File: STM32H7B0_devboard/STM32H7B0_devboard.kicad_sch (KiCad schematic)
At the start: 83 parts, among them J1 SWD, J2 24LC512 socet, J4 PORT_A, J5 PORT_B, J6 PORT_C, J7 PORT_D, J8 PORT_E, J9 Power_Conn, Q1 S8050, SW1 BOOT_SEL, U1 STM32H7B0VBT6, Y1 32.768KHz, Y2 25MHz

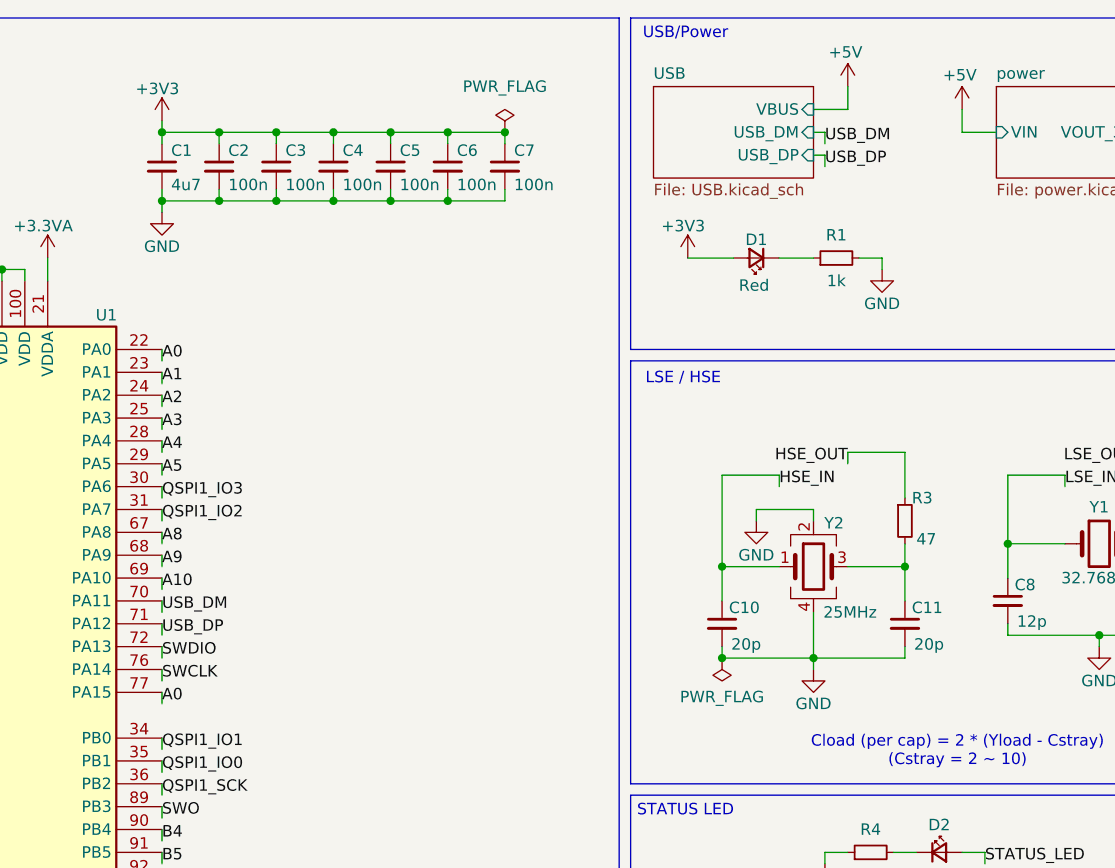
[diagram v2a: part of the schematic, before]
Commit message: Updated .gitignore
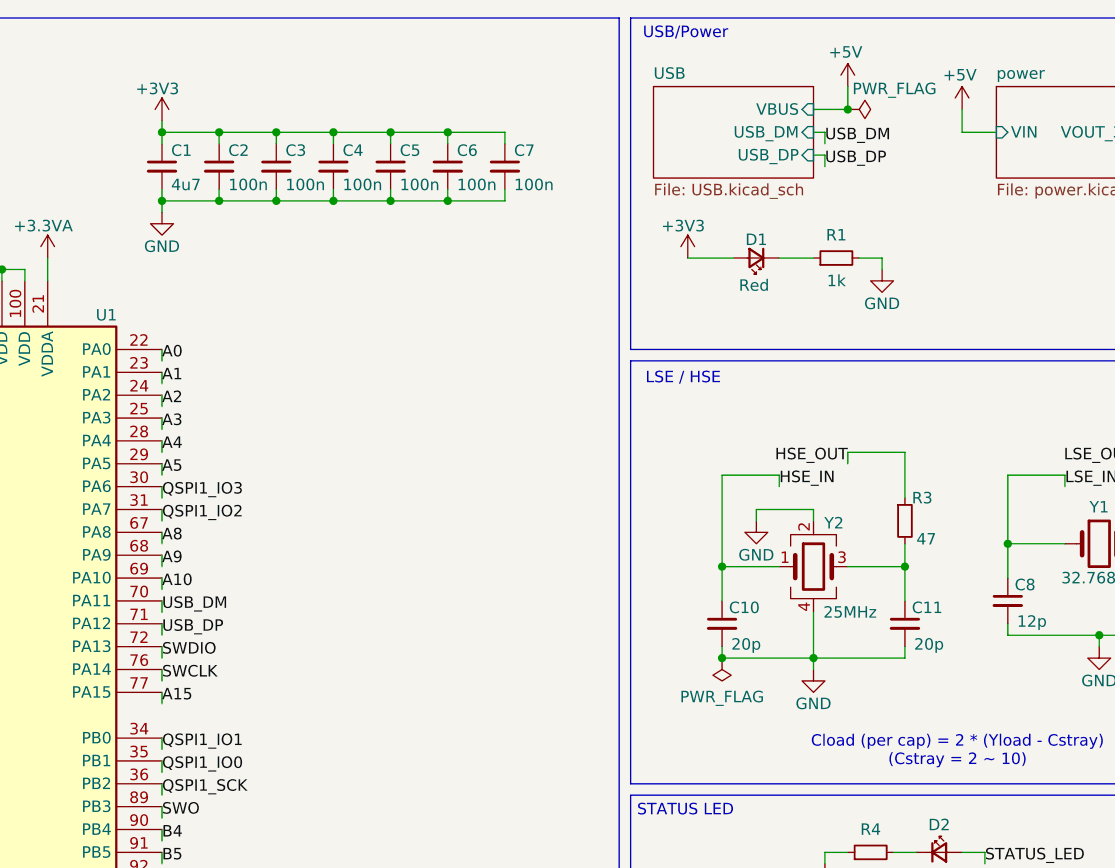
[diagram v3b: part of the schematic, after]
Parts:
- C14, C15: footprint Capacitor_SMD:C_1206_3216Metric -> Capacitor_SMD:C_0402_1005Metric
- R1, R4: footprint Resistor_SMD:R_0402_1005Metric -> Resistor_SMD:R_0603_1608Metric
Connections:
- net A0: no longer U1.77 (PA15)
- net A15: now also U1.77 (PA15)
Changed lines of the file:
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@@
 	)
 	(junction
-		(at 123.19 25.4)
-		(diameter 0)
-		(color 0 0 0 0)
-	)
-	(junction
 		(at 38.1 212.09)
 		(diameter 0)
@@
 	)
 	(junction
+		(at 161.29 22.86)
+		(diameter 0)
+		(color 0 0 0 0)
+	)
+	(junction
 		(at 49.53 269.24)
 		(diameter 0)
@@
 		)
 	)
-	(label "A0"
+	(label "A15"
 		(at 85.09 88.9 0)
 		(fields_autoplaced yes)
@@
 			)
 		)
-		(property "Footprint" "Resistor_SMD:R_0402_1005Metric"
+		(property "Footprint" "Resistor_SMD:R_0603_1608Metric"
 			(at 160.02 39.37 0)
 			(effects
@@
 	)
 	(symbol
+		(lib_id "power:PWR_FLAG")
+		(at 161.29 22.86 270)
+		(unit 1)
+		(exclude_from_sim no)
+		(in_bom yes)
+		(on_board yes)
+		(dnp no)
+		(property "Reference" "#FLG07"
+			(at 163.195 22.86 0)
+			(effects
+				(font
+					(size 1.27 1.27)
+				)
+				(hide yes)
+			)
+		)
+		(property "Value" "PWR_FLAG"
+			(at 161.798 20.574 90)
+			(effects
+				(font
+					(size 1.27 1.27)
+				)
+				(justify left)
+			)
+		)
+		(property "Footprint" ""
+			(at 161.29 22.86 0)
+			(effects
+				(font
+					(size 1.27 1.27)
+				)
+				(hide yes)
+			)
+		)
+		(property "Datasheet" "~"
+			(at 161.29 22.86 0)
+			(effects
+				(font
+					(size 1.27 1.27)
+				)
+				(hide yes)
+			)
+		)
+		(property "Description" "Special symbol for telling ERC where power comes from"
+			(at 161.29 22.86 0)
+			(effects
+				(font
+					(size 1.27 1.27)
+				)
+				(hide yes)
+			)
+		)
+		(pin "1"
+		)
+		(instances
+			(project "STM32H7B0_devboard"
+				(path "/0c02ba0f-c40f-484f-a270-dfb4a249f2e6"
+					(reference "#FLG07")
+					(unit 1)
+				)
+			)
+		)
+	)
+	(symbol
 		(lib_id "Device:R_Small")
 		(at 189.23 138.43 90)
@@
 			)
 		)
-		(property "Footprint" "Capacitor_SMD:C_1206_3216Metric"
+		(property "Footprint" "Capacitor_SMD:C_0402_1005Metric"
 			(at 95.25 210.82 0)
 			(effects
@@
 	)
 	(symbol
-		(lib_id "power:PWR_FLAG")
-		(at 123.19 25.4 0)
-		(unit 1)
-		(exclude_from_sim no)
-		(in_bom yes)
-		(on_board yes)
-		(dnp no)
-		(fields_autoplaced yes)
-		(property "Reference" "#FLG01"
-			(at 123.19 23.495 0)
-			(effects
-				(font
-					(size 1.27 1.27)
-				)
-				(hide yes)
-			)
-		)
-		(property "Value" "PWR_FLAG"
-			(at 123.19 20.32 0)
-			(effects
-				(font
-					(size 1.27 1.27)
-				)
-			)
-		)
-		(property "Footprint" ""
-			(at 123.19 25.4 0)
-			(effects
-				(font
-					(size 1.27 1.27)
-				)
-				(hide yes)
-			)
-		)
-		(property "Datasheet" "~"
-			(at 123.19 25.4 0)
-			(effects
-				(font
-					(size 1.27 1.27)
-				)
-				(hide yes)
-			)
-		)
-		(property "Description" "Special symbol for telling ERC where power comes from"
-			(at 123.19 25.4 0)
-			(effects
-				(font
-					(size 1.27 1.27)
-				)
-				(hide yes)
-			)
-		)
-		(pin "1"
-		)
-		(instances
-			(project "STM32H7B0_devboard"
-				(path "/0c02ba0f-c40f-484f-a270-dfb4a249f2e6"
-					(reference "#FLG01")
-					(unit 1)
-				)
-			)
-		)
-	)
-	(symbol
 		(lib_id "Device:R_Small")
 		(at 163.83 105.41 90)
@@
 			)
 		)
-		(property "Footprint" "Resistor_SMD:R_0402_1005Metric"
+		(property "Footprint" "Resistor_SMD:R_0603_1608Metric"
 			(at 163.83 105.41 0)
 			(effects
@@
 			)
 		)
-		(property "Footprint" "Capacitor_SMD:C_1206_3216Metric"
+		(property "Footprint" "Capacitor_SMD:C_0402_1005Metric"
 			(at 95.25 207.01 0)
 			(effects

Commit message: Started on layout
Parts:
- removed J9: Power_Conn, Connector_PinSocket_2.00mm:PinSocket_2x08_P2.00mm_Vertical, symbol Connector_Generic:Conn_02x08_Row_Letter_First
- added J9: Power_Conn, Connector_PinSocket_2.00mm:PinSocket_2x08_P2.00mm_Vertical, symbol Connector_Generic:Conn_02x08_Odd_Even
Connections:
- net +3V3: now also J9.2 (Pin_2), J9.4 (Pin_4), J9.6 (Pin_6), J9.8 (Pin_8)
- net +5V: now also J9.10 (Pin_10), J9.12 (Pin_12), J9.14 (Pin_14), J9.16 (Pin_16)
- net GND: now also J9.1 (Pin_1), J9.11 (Pin_11), J9.13 (Pin_13), J9.15 (Pin_15), J9.3 (Pin_3), J9.5 (Pin_5), J9.7 (Pin_7), J9.9 (Pin_9)
- net QSPI1_NSS: now also R11.1
- net at R23.2, U3.1 (NCS): no longer R11.1
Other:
- moved on the sheet: R11, R23, R24, R25

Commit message: Routing progress
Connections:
- net USB_DM renamed USB_DN
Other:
- sheet USB ports: added USB_DN; removed USB_DM
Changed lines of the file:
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@@
 		)
 	)
-	(label "USB_DM"
+	(label "USB_DN"
 		(at 158.75 26.67 0)
 		(fields_autoplaced yes)
@@
 		)
 	)
-	(label "USB_DM"
+	(label "USB_DN"
 		(at 85.09 78.74 0)
 		(fields_autoplaced yes)
@@
 		)
 	)
-	(label "USB_DM"
+	(label "USB_DN"
 		(at 226.06 48.26 180)
 		(fields_autoplaced yes)
@@
 			)
 		)
-		(pin "USB_DM" input
-			(at 157.48 25.4 0)
+		(pin "USB_DP" input
+			(at 157.48 27.94 0)
 			(effects
 				(font
@@
 			)
 		)
-		(pin "USB_DP" input
-			(at 157.48 27.94 0)
+		(pin "USB_DN" input
+			(at 157.48 25.4 0)
 			(effects
 				(font

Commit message: Done V1
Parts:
- C1, C15: LCSC (none) -> C307423
- C10, C11: LCSC (none) -> C1554
- C12, C13: LCSC (none) -> C343040
- C14, C2, C3, C4, C5, C6, C7: LCSC (none) -> C14445
- C16: LCSC (none) -> C913556
- C17: LCSC (none) -> C60133
- C8, C9: LCSC (none) -> C1547
- D1: LCSC (none) -> C965799
- D2: LCSC (none) -> C965807
- L1: LCSC (none) -> C74308
- Q1: LCSC (none) -> C916390
- R1: LCSC (none) -> C21190
- R10, R11, R15, R16, R9: LCSC (none) -> C25933
- R12: LCSC (none) -> C2849042
- R13: LCSC (none) -> C60490
- R14: LCSC (none) -> C11702
- R17, R18, R5, R6, R7, R8: LCSC (none) -> C25152
- R2, R3: LCSC (none) -> C25118
- R23, R24, R25, R26, R27, R28: LCSC (none) -> C115304
- R4: LCSC (none) -> C25989
- SW1: LCSC (none) -> C5962834
- U1: LCSC (none) -> C730227
- U3: LCSC (none) -> C5267629
- Y1: LCSC (none) -> C5213671
- Y2: LCSC (none) -> C13740

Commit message: Finished board
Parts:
- removed SW1: BOOT_SEL, Button_Switch_SMD:Nidec_Copal_CAS-120A, symbol Switch:SW_Nidec_CAS-120A1
- added JP21, JP22: ~, Jumper:SolderJumper-2_P1.3mm_Open_TrianglePad1.0x1.5mm, symbol Jumper:SolderJumper_2_Open
- added R29: 10k, Resistor_SMD:R_0402_1005Metric, symbol Device:R_Small
- C1, C15: LCSC C307423 -> C23733
- C12, C13: LCSC C343040 -> C12530
- C14, C2, C3, C4, C5, C6, C7: LCSC C14445 -> C1525
- C16: LCSC C913556 -> C52923
- C17: LCSC C60133 -> C15195
- D1: LCSC C965799 -> C2286
- D2: LCSC C965807 -> C72038
- Q1: LCSC C916390 -> C2146
- R10, R11, R15, R16, R9: LCSC C25933 -> C25879
- R13: LCSC C60490 -> C25744
- R14: LCSC C11702 -> C11702
- R17, R18, R5, R6, R7, R8: LCSC C25152 -> C25092
- R23, R24, R25, R26, R27, R28: LCSC C115304 -> C21189
- R4: LCSC C25989 -> C22843
- U3: now not fitted
- Y1: LCSC C5213671 -> C32346
- Y2: LCSC C13740 -> C9006
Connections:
- net +3V3: now also R29.2
- net BOOT0: now also JP21.1 (A), JP22.1 (A)
- net GND: now also JP22.2 (B)
- new net: JP21.2 (B), R29.1

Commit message: Copper balance
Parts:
- C10, C11: value 20p -> 12p; LCSC C1554 -> C1547
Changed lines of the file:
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@@
 			)
 		)
-		(property "Value" "20p"
+		(property "Value" "12p"
 			(at 148.336 82.296 0)
 			(effects
@@
 			)
 		)
-		(property "LCSC" "C1554"
+		(property "LCSC" "C1547"
 			(at 147.32 80.01 0)
 			(effects
@@
 			)
 		)
-		(property "Value" "20p"
+		(property "Value" "12p"
 			(at 168.656 82.296 0)
 			(effects
@@
 			)
 		)
-		(property "LCSC" "C1554"
+		(property "LCSC" "C1547"
 			(at 167.64 80.01 0)
 			(effects
